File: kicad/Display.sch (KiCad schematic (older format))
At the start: 33 parts

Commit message: Preperation for layout
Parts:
- removed Q? (x6): Q_PNP_BCE, symbol Q_PNP_BCE
- added P201, P204: CONN_01X07, Pin_Headers:Pin_Header_Straight_1x07, symbol CONN_01X07
- added P202, P203: CONN_01X06, Pin_Headers:Pin_Header_Straight_1x06, symbol CONN_01X06
- added Q201, Q202, Q203: BC856BS, SOT-363, symbol BC856BS
- R205, R206, R207, R208, R209, R210, R211, R212, R213, R214, R215, R216, R217: renamed from R?; footprint (none) -> Resistors_SMD:R_0805_HandSoldering
- U201: renamed from U?; MPN (none) -> SN74LS138NSR
- U202: renamed from U?; footprint (none) -> ClockFootprints:SOIC-16; MPN (none) -> CD4511BNSR
- gave numbers to parts that had none: 12
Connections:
- net labels added: C_Colon, C_Dig_0, C_Dig_1, C_Dig_2, C_Dig_3, C_Signal, D_Colon, D_Dig_0, D_Dig_1, D_Dig_2, D_Dig_3, D_Signal
- net labels removed: Colon, Signal
- wire segments 136 -> 148

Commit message: Started layout
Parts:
- Q201, Q202, Q203: footprint SOT-363 -> ClockFootprints:SOT-363
- U201: footprint (none) -> ClockFootprints:SOIC-16
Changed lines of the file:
@@
 F 0 "U201" H 1850 3900 60  0000 C CNN
 F 1 "SN74LS138" H 2050 2850 60  0000 C CNN
-F 2 "" H 1750 3400 60  0001 C CNN
+F 2 "ClockFootprints:SOIC-16" H 1750 3400 60  0001 C CNN
 F 3 "" H 1750 3400 60  0000 C CNN
 F 4 "SN74LS138NSR" H 1750 3400 60  0001 C CNN "MPN"
@@
 F 0 "Q202" H 3850 3125 50  0000 L CNN
 F 1 "BC856BS" H 3850 3050 50  0000 L CNN
-F 2 "SOT-363" H 3850 2975 50  0001 L CIN
+F 2 "ClockFootprints:SOT-363" H 3850 2975 50  0001 L CIN
 F 3 "" H 3650 3050 50  0000 L CNN
 F 4 "BC856BS" H 3650 3050 60  0001 C CNN "MPN"
@@
 F 0 "Q201" H 3800 3775 50  0000 L CNN
 F 1 "BC856BS" H 3800 3700 50  0000 L CNN
-F 2 "SOT-363" H 3800 3625 50  0001 L CIN
+F 2 "ClockFootprints:SOT-363" H 3800 3625 50  0001 L CIN
 F 3 "" H 3600 3700 50  0000 L CNN
 F 4 "BC856BS" H 3600 3700 60  0001 C CNN "MPN"
@@
 F 0 "Q201" H 3750 4475 50  0000 L CNN
 F 1 "BC856BS" H 3750 4400 50  0000 L CNN
-F 2 "SOT-363" H 3750 4325 50  0001 L CIN
+F 2 "ClockFootprints:SOT-363" H 3750 4325 50  0001 L CIN
 F 3 "" H 3550 4400 50  0000 L CNN
 F 4 "BC856BS" H 3550 4400 60  0001 C CNN "MPN"
@@
 F 0 "Q203" H 4850 3475 50  0000 L CNN
 F 1 "BC856BS" H 4850 3400 50  0000 L CNN
-F 2 "SOT-363" H 4850 3325 50  0001 L CIN
+F 2 "ClockFootprints:SOT-363" H 4850 3325 50  0001 L CIN
 F 3 "" H 4650 3400 50  0000 L CNN
 F 4 "BC856BS" H 4650 3400 60  0001 C CNN "MPN"
@@
 F 0 "Q202" H 4800 4125 50  0000 L CNN
 F 1 "BC856BS" H 4800 4050 50  0000 L CNN
-F 2 "SOT-363" H 4800 3975 50  0001 L CIN
+F 2 "ClockFootprints:SOT-363" H 4800 3975 50  0001 L CIN
 F 3 "" H 4600 4050 50  0000 L CNN
 F 4 "BC856BS" H 4600 4050 60  0001 C CNN "MPN"
@@
 F 0 "Q203" H 4850 4825 50  0000 L CNN
 F 1 "BC856BS" H 4850 4750 50  0000 L CNN
-F 2 "SOT-363" H 4850 4675 50  0001 L CIN
+F 2 "ClockFootprints:SOT-363" H 4850 4675 50  0001 L CIN
 F 3 "" H 4650 4750 50  0000 L CNN
 F 4 "BC856BS" H 4650 4750 60  0001 C CNN "MPN"

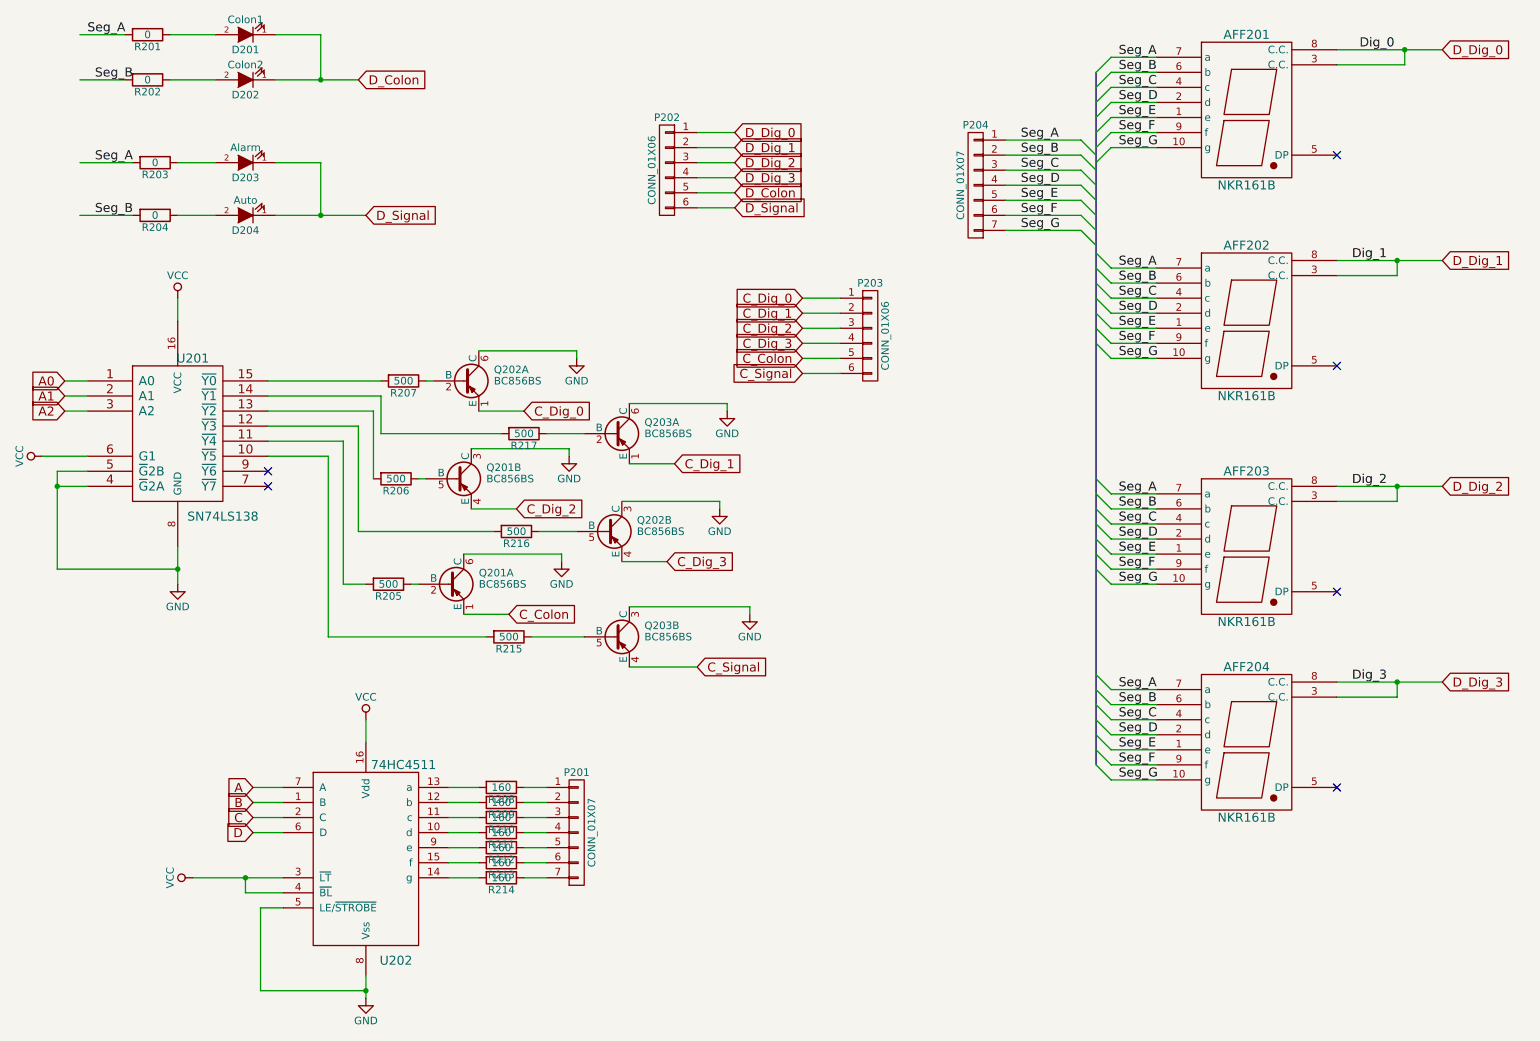
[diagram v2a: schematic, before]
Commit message: Updated the layout for the controller side
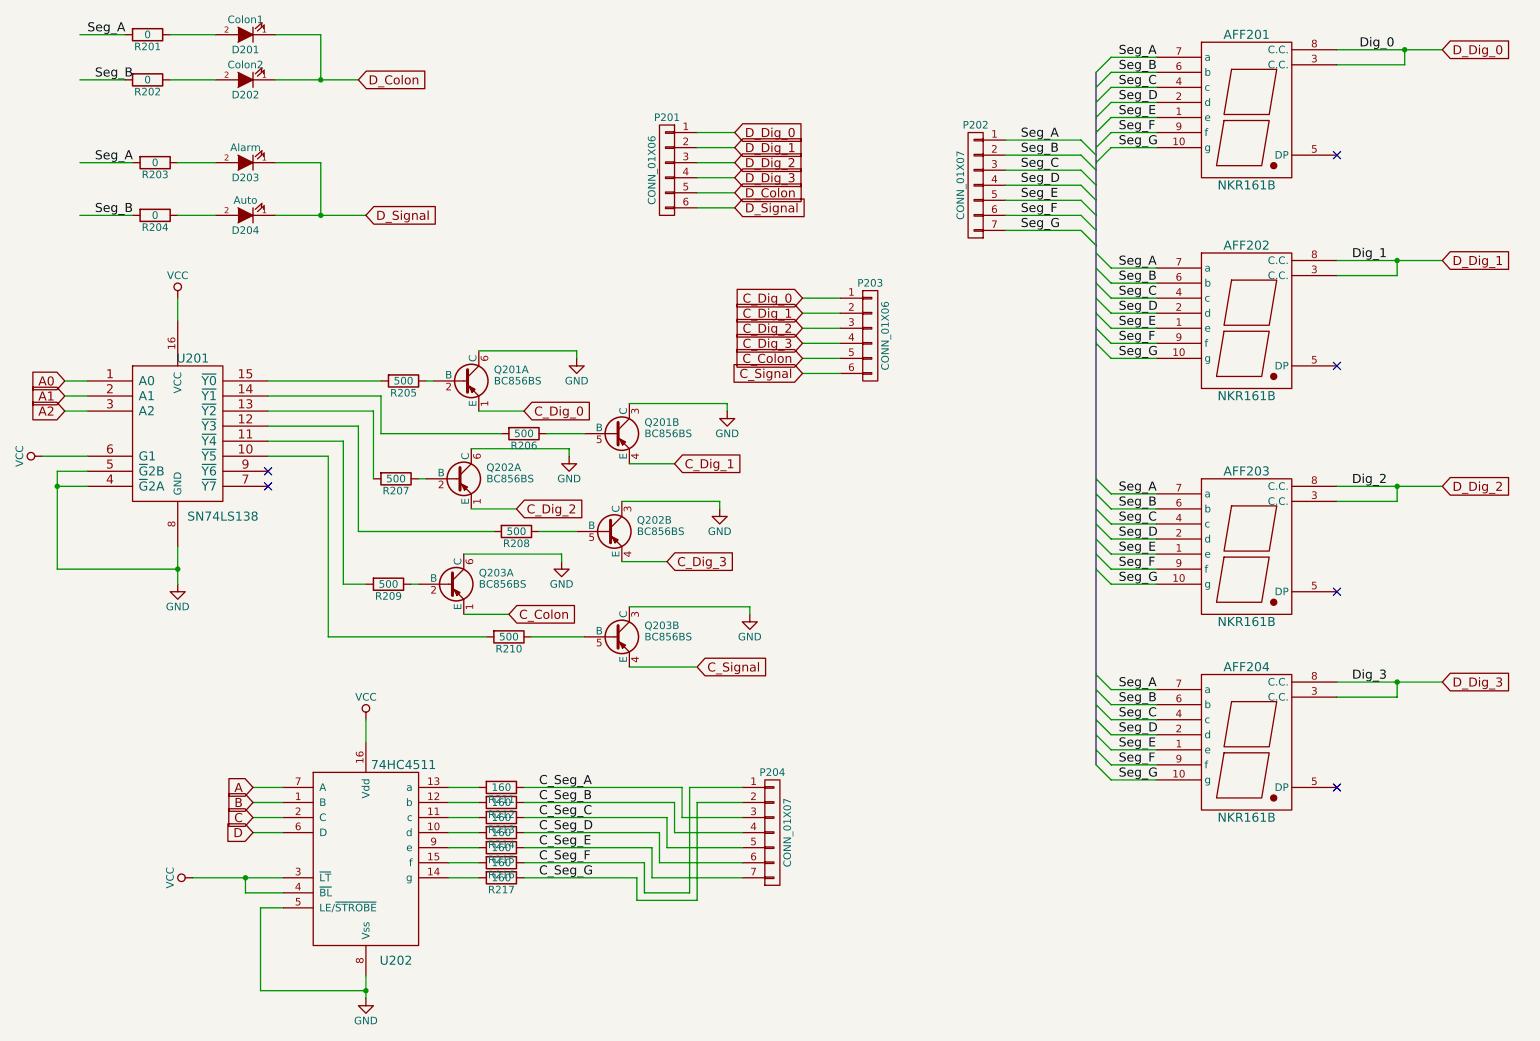
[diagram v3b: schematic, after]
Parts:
- renumbered P202 to P201, P204 to P202, P201 to P204, Q202 to Q201, Q203 to Q201, Q201 to Q202, Q201 to Q203, R207 to R205, R217 to R206, R206 to R207, R216 to R208, R205 to R209, R215 to R210, R208 to R211, R209 to R212, R210 to R213, R211 to R214, R212 to R215, R213 to R216, R214 to R217
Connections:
- net C_Dig_1: now also Q201.4 (E); no longer Q201.1 (E)
- net C_Dig_2: now also Q202.1 (E); no longer Q202.4 (E)
- net GND: now also Q201.3 (C), Q202.6 (C); no longer Q201.6 (C), Q202.3 (C)
- net C_Seg_A: now reaches R211.1
- net C_Seg_A: now also P204.3 (P3); no longer P204.1 (P1)
- net C_Seg_B: now reaches R212.1
- net C_Seg_B: now also P204.4 (P4); no longer P204.2 (P2)
- net C_Seg_C: now reaches R213.1
- net C_Seg_C: now also P204.5 (P5); no longer P204.3 (P3)
- net C_Seg_D: now reaches R214.1
- net C_Seg_D: now also P204.6 (P6); no longer P204.4 (P4)
- net C_Seg_E: now reaches R215.1
- net C_Seg_E: now also P204.7 (P7); no longer P204.5 (P5)
- net C_Seg_F: now reaches R216.1
- net C_Seg_F: now also P204.1 (P1); no longer P204.6 (P6)
- net C_Seg_G: now reaches R217.1
- net C_Seg_G: now also P204.2 (P2); no longer P204.7 (P7)
- net at R206.1: now also Q201.5 (B); no longer Q201.2 (B)
- net at R207.1: now also Q202.2 (B); no longer Q202.5 (B)
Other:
- moved on the sheet: P204
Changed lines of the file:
@@
 $EndComp
 $Comp
-L R R207
+L R R205
 U 1 1 55873377
 P 3250 3050
-F 0 "R207" V 3330 3050 50  0000 C CNN
+F 0 "R205" V 3330 3050 50  0000 C CNN
 F 1 "500" V 3250 3050 50  0000 C CNN
 F 2 "Resistors_SMD:R_0805_HandSoldering" V 3180 3050 30  0001 C CNN
@@
 	3400 3050 3450 3050
 $Comp
-L R R208
+L R R211
 U 1 1 5587356B
 P 3900 5750
-F 0 "R208" V 3980 5750 50  0000 C CNN
+F 0 "R211" V 3980 5750 50  0000 C CNN
 F 1 "160" V 3900 5750 50  0000 C CNN
 F 2 "Resistors_SMD:R_0805_HandSoldering" V 3830 5750 30  0001 C CNN
@@
 $EndComp
 $Comp
-L R R209
+L R R212
 U 1 1 55873774
 P 3900 5850
-F 0 "R209" V 3980 5850 50  0000 C CNN
+F 0 "R212" V 3980 5850 50  0000 C CNN
 F 1 "160" V 3900 5850 50  0000 C CNN
 F 2 "Resistors_SMD:R_0805_HandSoldering" V 3830 5850 30  0001 C CNN
@@
 $EndComp
 $Comp
-L R R210
+L R R213
 U 1 1 5587381A
 P 3900 5950
-F 0 "R210" V 3980 5950 50  0000 C CNN
+F 0 "R213" V 3980 5950 50  0000 C CNN
 F 1 "160" V 3900 5950 50  0000 C CNN
 F 2 "Resistors_SMD:R_0805_HandSoldering" V 3830 5950 30  0001 C CNN
@@
 $EndComp
 $Comp
-L R R211
+L R R214
 U 1 1 55873877
 P 3900 6050
-F 0 "R211" V 3980 6050 50  0000 C CNN
+F 0 "R214" V 3980 6050 50  0000 C CNN
 F 1 "160" V 3900 6050 50  0000 C CNN
 F 2 "Resistors_SMD:R_0805_HandSoldering" V 3830 6050 30  0001 C CNN
@@
 $EndComp
 $Comp
-L R R212
+L R R215
 U 1 1 55873973
 P 3900 6150
-F 0 "R212" V 3980 6150 50  0000 C CNN
+F 0 "R215" V 3980 6150 50  0000 C CNN
 F 1 "160" V 3900 6150 50  0000 C CNN
 F 2 "Resistors_SMD:R_0805_HandSoldering" V 3830 6150 30  0001 C CNN
@@
 $EndComp
 $Comp
-L R R213
+L R R216
 U 1 1 558739F1
 P 3900 6250
-F 0 "R213" V 3980 6250 50  0000 C CNN
+F 0 "R216" V 3980 6250 50  0000 C CNN
 F 1 "160" V 3900 6250 50  0000 C CNN
 F 2 "Resistors_SMD:R_0805_HandSoldering" V 3830 6250 30  0001 C CNN
@@
 $EndComp
 $Comp
-L R R214
+L R R217
 U 1 1 55873A73
 P 3900 6350
-F 0 "R214" V 3980 6350 50  0000 C CNN
+F 0 "R217" V 3980 6350 50  0000 C CNN
 F 1 "160" V 3900 6350 50  0000 C CNN
 F 2 "Resistors_SMD:R_0805_HandSoldering" V 3830 6350 30  0001 C CNN
@@
 	0    1    1    0
 $EndComp
-Wire Wire Line
-	4050 5750 4200 5750
-Wire Wire Line
-	4200 5850 4050 5850
-Wire Wire Line
-	4050 5950 4200 5950
-Wire Wire Line
-	4200 6050 4050 6050
-Wire Wire Line
-	4050 6150 4200 6150
-Wire Wire Line
-	4200 6250 4050 6250
-Wire Wire Line
-	4050 6350 4200 6350
 Wire Wire Line
 	3750 3250 4050 3250
@@
 $EndComp
 $Comp
-L R R217
+L R R206
 U 1 1 558747A2
 P 4050 3400
-F 0 "R217" V 4130 3400 50  0000 C CNN
+F 0 "R206" V 4130 3400 50  0000 C CNN
 F 1 "500" V 4050 3400 50  0000 C CNN
 F 2 "Resistors_SMD:R_0805_HandSoldering" V 3980 3400 30  0001 C CNN
@@
 $EndComp
 $Comp
-L R R206
+L R R207
 U 1 1 55874B76
 P 3200 3700
-F 0 "R206" V 3280 3700 50  0000 C CNN
+F 0 "R207" V 3280 3700 50  0000 C CNN
 F 1 "500" V 3200 3700 50  0000 C CNN
 F 2 "Resistors_SMD:R_0805_HandSoldering" V 3130 3700 30  0001 C CNN
@@
 $EndComp
 $Comp
-L R R216
+L R R208
 U 1 1 55874B8E
 P 4000 4050
-F 0 "R216" V 4080 4050 50  0000 C CNN
+F 0 "R208" V 4080 4050 50  0000 C CNN
 F 1 "500" V 4000 4050 50  0000 C CNN
 F 2 "Resistors_SMD:R_0805_HandSoldering" V 3930 4050 30  0001 C CNN
@@
 $EndComp
 $Comp
-L R R205
+L R R209
 U 1 1 5587592B
 P 3150 4400
-F 0 "R205" V 3230 4400 50  0000 C CNN
+F 0 "R209" V 3230 4400 50  0000 C CNN
 F 1 "500" V 3150 4400 50  0000 C CNN
 F 2 "Resistors_SMD:R_0805_HandSoldering" V 3080 4400 30  0001 C CNN
@@
 $EndComp
 $Comp
-L R R215
+L R R210
 U 1 1 55875943
 P 3950 4750
-F 0 "R215" V 4030 4750 50  0000 C CNN
+F 0 "R210" V 4030 4750 50  0000 C CNN
 F 1 "500" V 3950 4750 50  0000 C CNN
 F 2 "Resistors_SMD:R_0805_HandSoldering" V 3880 4750 30  0001 C CNN
@@
 Connection ~ 3000 7100
 $Comp
-L CONN_01X07 P204
+L CONN_01X07 P202
 U 1 1 55899A95
 P 7050 1750
-F 0 "P204" H 7050 2150 50  0000 C CNN
+F 0 "P202" H 7050 2150 50  0000 C CNN
 F 1 "CONN_01X07" V 7150 1750 50  0000 C CNN
 F 2 "Pin_Headers:Pin_Header_Straight_1x07" H 7050 1750 60  0001 C CNN
@@
 Seg_B
 $Comp
-L CONN_01X06 P202
+L CONN_01X06 P201
 U 1 1 5589B385
 P 5000 1650
-F 0 "P202" H 5000 2000 50  0000 C CNN
+F 0 "P201" H 5000 2000 50  0000 C CNN
 F 1 "CONN_01X06" V 5100 1650 50  0000 C CNN
 F 2 "Pin_Headers:Pin_Header_Straight_1x06" H 5000 1650 60  0001 C CNN
@@
 	5450 1900 5200 1900
 $Comp
-L CONN_01X07 P201
+L CONN_01X07 P204
 U 1 1 5589E0CB
-P 4400 6050
-F 0 "P201" H 4400 6450 50  0000 C CNN
-F 1 "CONN_01X07" V 4500 6050 50  0000 C CNN
-F 2 "Pin_Headers:Pin_Header_Straight_1x07" H 4400 6050 60  0001 C CNN
-F 3 "" H 4400 6050 60  0000 C CNN
-	1    4400 6050
+P 5700 6050
+F 0 "P204" H 5700 6450 50  0000 C CNN
+F 1 "CONN_01X07" V 5800 6050 50  0000 C CNN
+F 2 "Pin_Headers:Pin_Header_Straight_1x07" H 5700 6050 60  0001 C CNN
+F 3 "" H 5700 6050 60  0000 C CNN
+	1    5700 6050
 	1    0    0    -1
 $EndComp
@@
 	6150 3000 5900 3000
 $Comp
-L BC856BS Q202
+L BC856BS Q201
 U 1 1 558A038F
 P 3650 3050
-F 0 "Q202" H 3850 3125 50  0000 L CNN
+F 0 "Q201" H 3850 3125 50  0000 L CNN
 F 1 "BC856BS" H 3850 3050 50  0000 L CNN
 F 2 "ClockFootprints:SOT-363" H 3850 2975 50  0001 L CIN
@@
 $EndComp
 $Comp
-L BC856BS Q201
-U 2 1 558A04DE
+L BC856BS Q202
+U 1 1 558A04DE
 P 3600 3700
-F 0 "Q201" H 3800 3775 50  0000 L CNN
+F 0 "Q202" H 3800 3775 50  0000 L CNN
 F 1 "BC856BS" H 3800 3700 50  0000 L CNN
 F 2 "ClockFootprints:SOT-363" H 3800 3625 50  0001 L CIN
 F 3 "" H 3600 3700 50  0000 L CNN
 F 4 "BC856BS" H 3600 3700 60  0001 C CNN "MPN"
-	2    3600 3700
-	1    0    0    -1
-$EndComp
-$Comp
-L BC856BS Q201
+	1    3600 3700
+	1    0    0    -1
+$EndComp
+$Comp
+L BC856BS Q203
 U 1 1 558A05C1
 P 3550 4400
-F 0 "Q201" H 3750 4475 50  0000 L CNN
+F 0 "Q203" H 3750 4475 50  0000 L CNN
 F 1 "BC856BS" H 3750 4400 50  0000 L CNN
 F 2 "ClockFootprints:SOT-363" H 3750 4325 50  0001 L CIN
@@
 $EndComp
 $Comp
-L BC856BS Q203
-U 1 1 558A074D
+L BC856BS Q201
+U 2 1 558A074D
 P 4650 3400
-F 0 "Q203" H 4850 3475 50  0000 L CNN
+F 0 "Q201" H 4850 3475 50  0000 L CNN
 F 1 "BC856BS" H 4850 3400 50  0000 L CNN
 F 2 "ClockFootprints:SOT-363" H 4850 3325 50  0001 L CIN
 F 3 "" H 4650 3400 50  0000 L CNN
 F 4 "BC856BS" H 4650 3400 60  0001 C CNN "MPN"
-	1    4650 3400
+	2    4650 3400
 	1    0    0    -1
 $EndComp
@@
 	1    0    0    -1
 $EndComp
+Text Label 4150 5750 0    60   ~ 0
+C_Seg_A
+Text Label 4150 5850 0    60   ~ 0
+C_Seg_B
+Text Label 4150 5950 0    60   ~ 0
+C_Seg_C
+Text Label 4150 6050 0    60   ~ 0
+C_Seg_D
+Text Label 4150 6150 0    60   ~ 0
+C_Seg_E
+Text Label 4150 6250 0    60   ~ 0
+C_Seg_F
+Text Label 4150 6350 0    60   ~ 0
+C_Seg_G
+Wire Wire Line
+	5150 5750 5150 6450
+Wire Wire Line
+	5150 5750 5500 5750
+Wire Wire Line
+	5200 5850 5200 6500
+Wire Wire Line
+	5200 5850 5500 5850
+Wire Wire Line
+	4050 5750 5100 5750
+Wire Wire Line
+	5100 5750 5100 5950
+Wire Wire Line
+	5100 5950 5500 5950
+Wire Wire Line
+	4050 5850 5050 5850
+Wire Wire Line
+	5050 5850 5050 6050
+Wire Wire Line
+	5050 6050 5500 6050
+Wire Wire Line
+	4050 5950 5000 5950
+Wire Wire Line
+	5000 5950 5000 6150
+Wire Wire Line
+	5000 6150 5500 6150
+Wire Wire Line
+	4050 6350 4800 6350
+Wire Wire Line
+	4800 6350 4800 6500
+Wire Wire Line
+	4800 6500 5200 6500
+Wire Wire Line
+	4050 6250 4850 6250
+Wire Wire Line
+	4850 6250 4850 6450
+Wire Wire Line
+	4850 6450 5150 6450
+Wire Wire Line
+	4050 6050 4950 6050
+Wire Wire Line
+	4950 6050 4950 6250
+Wire Wire Line
+	4950 6250 5500 6250
+Wire Wire Line
+	4050 6150 4900 6150
+Wire Wire Line
+	4900 6150 4900 6350
+Wire Wire Line
+	4900 6350 5500 6350
 $EndSCHEMATC
